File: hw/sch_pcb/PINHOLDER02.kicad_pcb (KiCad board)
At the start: 2 copper layers, 60.6 x 60.4 mm, 7 parts, among them J1 HEADER_1x03, M2 HOLE, M3 HOLE, M4 HOLE

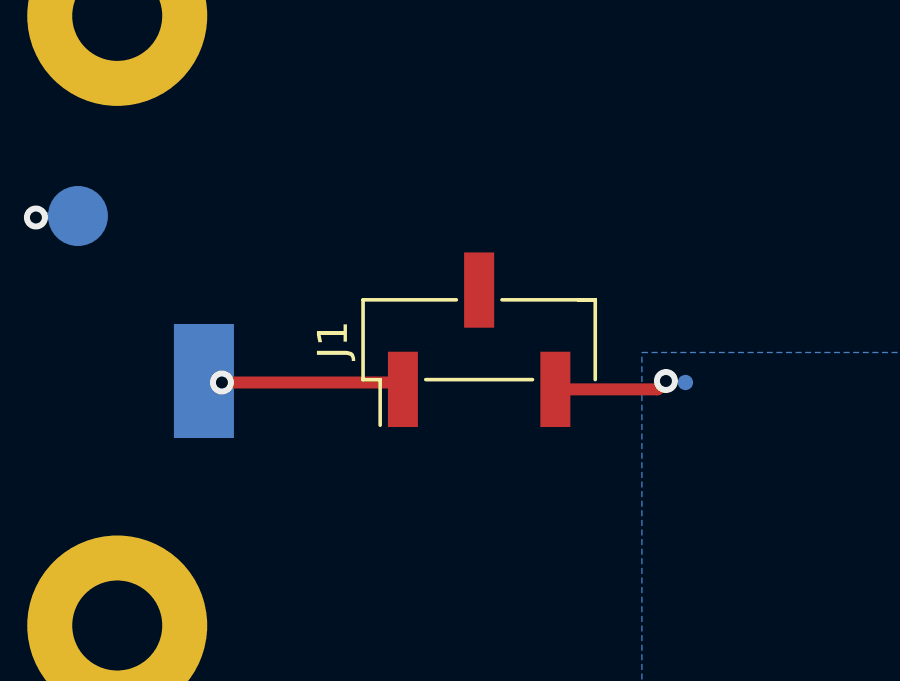
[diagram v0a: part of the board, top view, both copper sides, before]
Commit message: zamena anoda-katoda
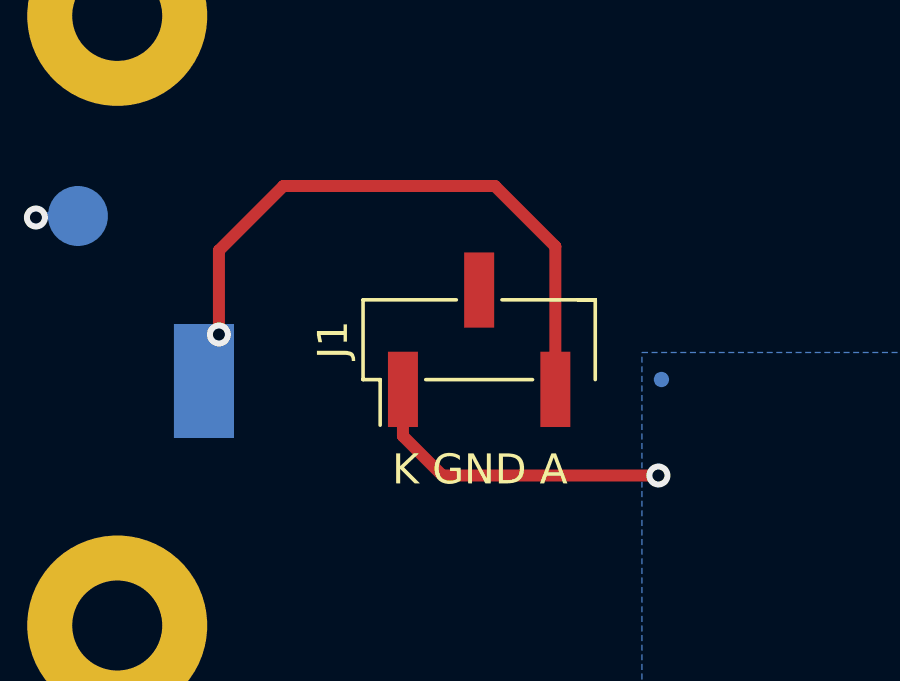
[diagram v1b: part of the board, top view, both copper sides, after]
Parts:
- moved TP1 0.81 mm to (167.8, 88.6)
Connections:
- J1 pad 1: Net-(J1-Pad1) -> /circle_0
- J1 pad 3: /circle_0 -> Net-(J1-Pad3)
- TP2 pad 1: Net-(J1-Pad1) -> Net-(J1-Pad3)
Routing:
- net Net-(J1-Pad3): track 0.00 -> 20.5 mm, vias 0 -> 1
- net /circle_0: track 3.87 -> 10.9 mm
- net Net-(J1-Pad1): track 6.13 -> 0.00 mm, vias 1 -> 0
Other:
- board text added: "A"
- board text added: "K GND A"
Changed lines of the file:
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@@
   (net 1 "/circle_0")
   (net 2 "GND")
-  (net 3 "Net-(J1-Pad1)")
+  (net 3 "Net-(J1-Pad3)")
   (footprint "Mlab_Mechanical:MountingHole_3mm" placed (layer "F.Cu")
     (at 149.61 76.48)
@@
     (fp_line (start 2.54 0.32) (end 1.27 0.32) (layer "F.Fab") (width 0.1))
     (pad "1" smd rect locked (at -1.655 -2.54 90) (size 2.51 1) (layers "F.Cu" "F.Paste" "F.Mask")
-      (net 3 "Net-(J1-Pad1)") (pintype "input"))
+      (net 1 "/circle_0") (pintype "input"))
     (pad "2" smd rect locked (at 1.655 0 90) (size 2.51 1) (layers "F.Cu" "F.Paste" "F.Mask")
       (net 2 "GND") (pintype "input"))
     (pad "3" smd rect locked (at -1.655 2.54 90) (size 2.51 1) (layers "F.Cu" "F.Paste" "F.Mask")
-      (net 1 "/circle_0") (pintype "input"))
+      (net 3 "Net-(J1-Pad3)") (pintype "input"))
     (model "${KICAD6_3DMODEL_DIR}/Connector_PinHeader_2.54mm.3dshapes/PinHeader_1x03_P2.54mm_Vertical_SMD_Pin1Left.wrl"
       (offset (xyz 0 0 0))
@@
   )
   (footprint "Mlab_CON:TestPoint_Pad_D0.5mm_noSilk" (layer "B.Cu")
-    (at 168.55 88.7 180)
+    (at 167.75 88.6 180)
     (descr "SMD pad as test Point, diameter 1.0mm")
     (tags "test point SMD pad")
@@
     (fp_line (start 0 -0.5) (end 0 -1) (layer "B.Fab") (width 0.15))
     (pad "1" smd rect (at 0 0 90) (size 3.8 2) (layers "B.Cu" "B.Paste" "B.Mask")
-      (net 3 "Net-(J1-Pad1)") (pinfunction "1") (pintype "passive"))
+      (net 3 "Net-(J1-Pad3)") (pinfunction "1") (pintype "passive"))
     (model "${KICAD6_3DMODEL_DIR}/TestPoint.3dshapes/TestPoint_Keystone_5019_Minature.wrl"
       (offset (xyz 0 0 0))
@@
   )
   (gr_text "GND" (at 148.25 85.85) (layer "B.SilkS")
-    (effects (font (size 1.5 1.5) (thickness 0.3)) (justify mirror))
+    (effects (font (size 1 1) (thickness 0.25)) (justify mirror))
   )
   (gr_text "MLAB.cz" (at 160.024 74.8925) (layer "B.SilkS")
     (effects (font (size 1.5 1.5) (thickness 0.3)) (justify mirror))
   )
+  (gr_text "A" (at 150.25 88.85 90) (layer "B.SilkS")
+    (effects (font (size 1 1) (thickness 0.15)) (justify mirror))
+  )
   (gr_text "PINHOLDER02A" (at 175.5 74.8) (layer "F.SilkS")
     (effects (font (size 1.7 1.7) (thickness 0.3)))
@@
     (effects (font (size 1.5 1.5) (thickness 0.3)))
   )
-  (segment (start 164.214 88.929) (end 167.621 88.929) (width 0.4) (layer "F.Cu") (net 1))
-  (segment (start 167.621 88.929) (end 167.9 88.65) (width 0.4) (layer "F.Cu") (net 1))
-  (via (at 167.9 88.65) (size 0.8) (drill 0.4) (layers "F.Cu" "B.Cu") (net 1))
-  (segment (start 167.95 88.7) (end 167.9 88.65) (width 0.25) (layer "B.Cu") (net 1))
+  (gr_text "K GND A" (at 161.7 91.6) (layer "F.SilkS")
+    (effects (font (size 1 1) (thickness 0.15)))
+  )
+  (segment (start 167.65 91.8) (end 160.45 91.8) (width 0.4) (layer "F.Cu") (net 1))
+  (segment (start 160.45 91.8) (end 159.134 90.484) (width 0.4) (layer "F.Cu") (net 1))
+  (segment (start 159.134 88.929) (end 158.905 88.7) (width 0.4) (layer "F.Cu") (net 1))
+  (segment (start 159.134 90.484) (end 159.134 88.929) (width 0.4) (layer "F.Cu") (net 1))
+  (via (at 167.65 91.8) (size 0.8) (drill 0.4) (layers "F.Cu" "B.Cu") (net 1))
   (via (at 146.9 83.2) (size 0.8) (drill 0.4) (layers "F.Cu" "B.Cu") (net 2))
   (segment (start 146.9 83.2) (end 146.95 83.15) (width 0.25) (layer "B.Cu") (net 2))
   (segment (start 146.95 83.15) (end 148.3 83.15) (width 0.25) (layer "B.Cu") (net 2))
-  (segment (start 158.905 88.7) (end 153.1 88.7) (width 0.4) (layer "F.Cu") (net 3))
-  (segment (start 159.134 88.929) (end 158.905 88.7) (width 0.4) (layer "F.Cu") (net 3))
-  (via (at 153.1 88.7) (size 0.8) (drill 0.4) (layers "F.Cu" "B.Cu") (net 3))
+  (segment (start 153 87.1) (end 153 84.3) (width 0.4) (layer "F.Cu") (net 3))
+  (segment (start 155.15 82.15) (end 162.2 82.15) (width 0.4) (layer "F.Cu") (net 3))
+  (segment (start 164.214 84.164) (end 164.214 88.929) (width 0.4) (layer "F.Cu") (net 3))
+  (segment (start 162.2 82.15) (end 164.214 84.164) (width 0.4) (layer "F.Cu") (net 3))
+  (segment (start 153 84.3) (end 155.15 82.15) (width 0.4) (layer "F.Cu") (net 3))
+  (via (at 153 87.1) (size 0.8) (drill 0.4) (layers "F.Cu" "B.Cu") (net 3))
   (zone (net 2) (net_name "GND") (layer "F.Cu") (hatch edge 0.508)
     (connect_pads (clearance 0.4))

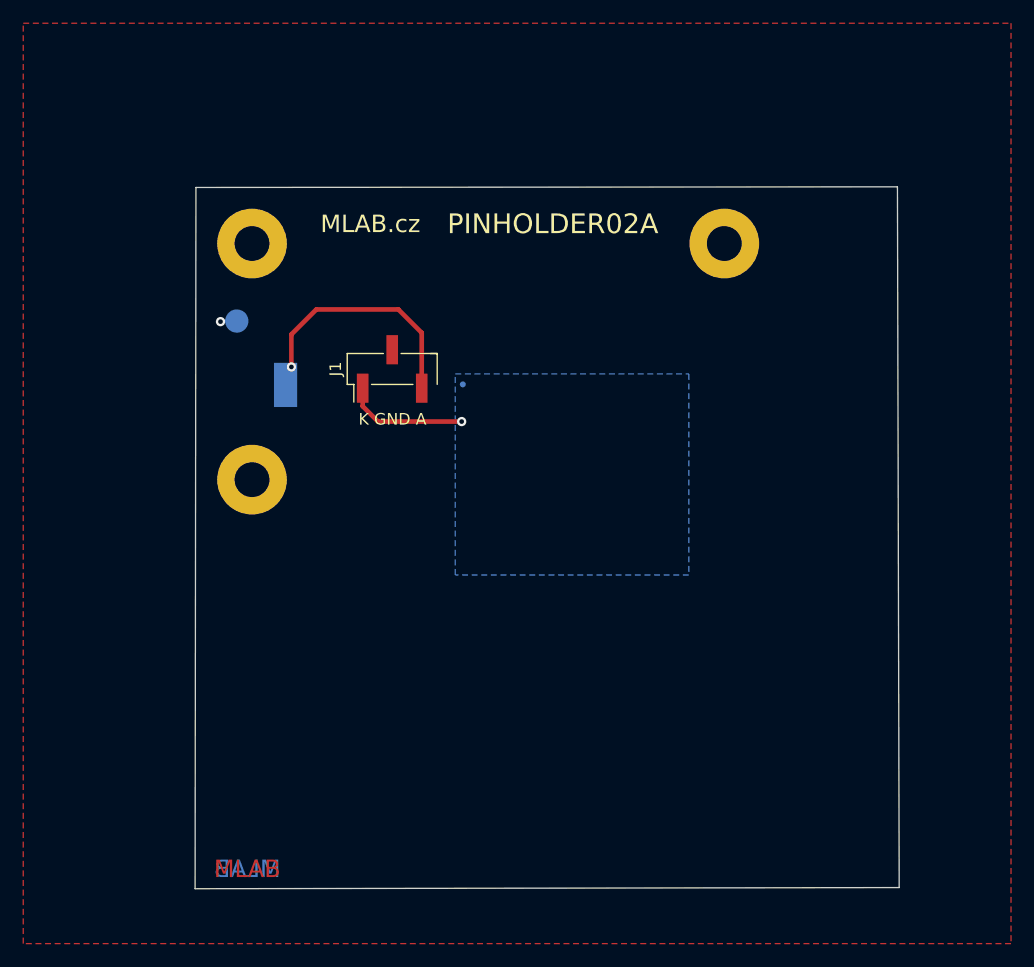
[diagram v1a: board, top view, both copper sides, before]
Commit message: Fix shape to be ortogonal.
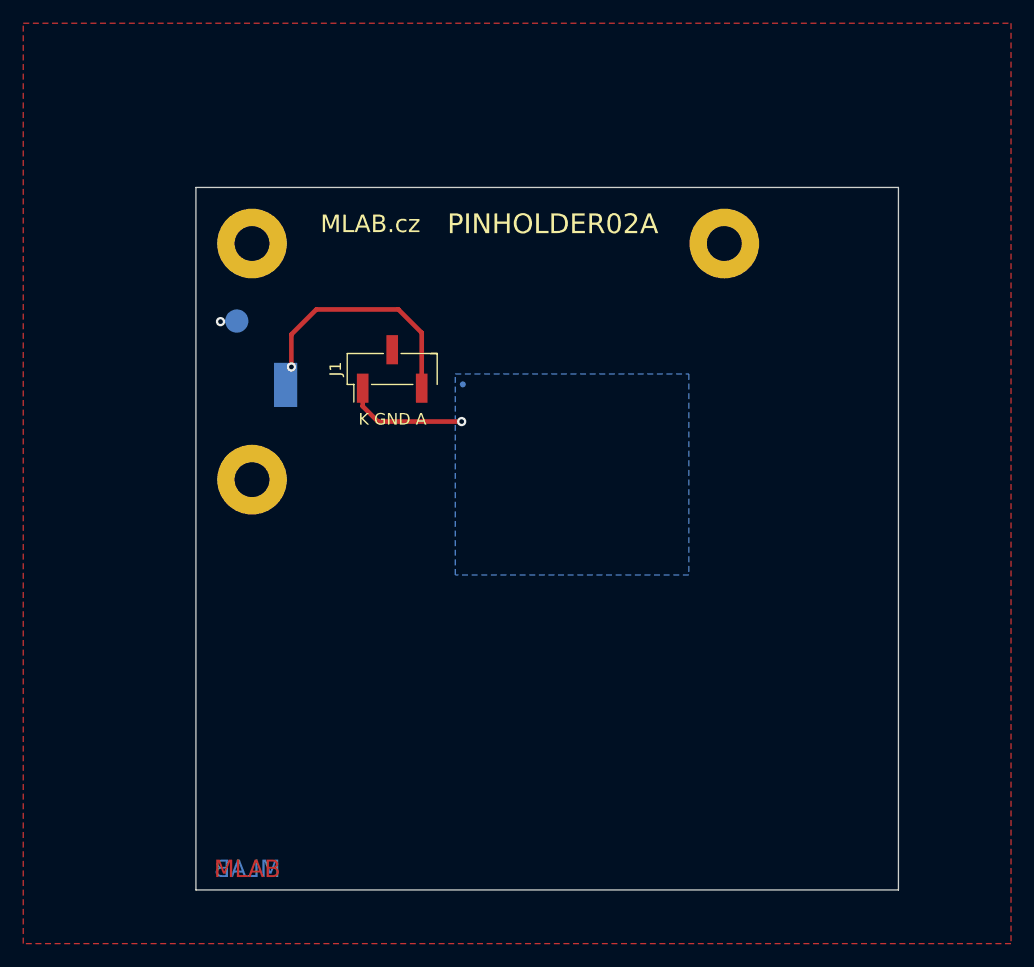
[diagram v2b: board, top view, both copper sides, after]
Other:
- board size 60.6 x 60.4 mm -> 60.5 x 60.5 mm
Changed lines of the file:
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@@
   (setup
     (pad_to_mask_clearance 0)
+    (aux_axis_origin 149.61 76.48)
     (pcbplotparams
       (layerselection 0x00010fc_ffffffff)
@@
     )
   )
-  (gr_line (start 144.712 132) (end 205.3 131.9) (layer "Edge.Cuts") (width 0.1))
-  (gr_line (start 144.786 71.656) (end 205.15 71.6) (layer "Edge.Cuts") (width 0.1))
-  (gr_line (start 205.15 71.6) (end 205.3 131.9) (layer "Edge.Cuts") (width 0.1))
-  (gr_line (start 144.712 132) (end 144.786 71.656) (layer "Edge.Cuts") (width 0.1))
+  (gr_line (start 144.784 132.106) (end 205.236 132.106) (layer "Edge.Cuts") (width 0.1))
+  (gr_line (start 144.784 71.654) (end 205.236 71.654) (layer "Edge.Cuts") (width 0.1))
+  (gr_line (start 205.236 71.654) (end 205.236 132.106) (layer "Edge.Cuts") (width 0.1))
+  (gr_line (start 144.784 132.106) (end 144.784 71.654) (layer "Edge.Cuts") (width 0.1))
   (gr_rect (start 134.8 78.6) (end 146.2 90.4) (layer "User.1") (width 0.15) (fill solid))
   (gr_line (start 146.6 78.2) (end 146.6 90.8) (layer "User.2") (width 1))
@@
     (effects (font (size 1 1) (thickness 0.15)))
   )
+  (dimension (type aligned) (layer "Cmts.User")
+    (pts (xy 144.784 132.106) (xy 205.236 132.106))
+    (height 3.784)
+    (gr_text "60,4520 mm" (at 175.01 134.74) (layer "Cmts.User")
+      (effects (font (size 1 1) (thickness 0.15)))
+    )
+    (format (units 3) (units_format 1) (precision 4))
+    (style (thickness 0.15) (arrow_length 1.27) (text_position_mode 0) (extension_height 0.58642) (extension_offset 0.5) keep_text_aligned)
+  )
+  (dimension (type aligned) (layer "Cmts.User")
+    (pts (xy 144.784 71.654) (xy 205.236 71.654))
+    (height -6.884)
+    (gr_text "60,4520 mm" (at 175.01 63.62) (layer "Cmts.User")
+      (effects (font (size 1 1) (thickness 0.15)))
+    )
+    (format (units 3) (units_format 1) (precision 4))
+    (style (thickness 0.15) (arrow_length 1.27) (text_position_mode 0) (extension_height 0.58642) (extension_offset 0.5) keep_text_aligned)
+  )
+  (dimension (type aligned) (layer "Cmts.User")
+    (pts (xy 205.236 132.106) (xy 205.236 71.654))
+    (height 6.854)
+    (gr_text "60,4520 mm" (at 210.94 101.88 90) (layer "Cmts.User")
+      (effects (font (size 1 1) (thickness 0.15)))
+    )
+    (format (units 3) (units_format 1) (precision 4))
+    (style (thickness 0.15) (arrow_length 1.27) (text_position_mode 0) (extension_height 0.58642) (extension_offset 0.5) keep_text_aligned)
+  )
+  (dimension (type aligned) (layer "Cmts.User")
+    (pts (xy 149.61 76.48) (xy 149.61 96.8))
+    (height 11.18)
+    (gr_text "20,3200 mm" (at 137.28 86.64 90) (layer "Cmts.User")
+      (effects (font (size 1 1) (thickness 0.15)))
+    )
+    (format (units 3) (units_format 1) (precision 4))
+    (style (thickness 0.15) (arrow_length 1.27) (text_position_mode 0) (extension_height 0.58642) (extension_offset 0.5) keep_text_aligned)
+  )
+  (dimension (type aligned) (layer "Cmts.User")
+    (pts (xy 144.784 132.106) (xy 144.784 71.654))
+    (height -10.164)
+    (gr_text "60,4520 mm" (at 133.47 101.88 90) (layer "Cmts.User")
+      (effects (font (size 1 1) (thickness 0.15)))
+    )
+    (format (units 3) (units_format 1) (precision 4))
+    (style (thickness 0.15) (arrow_length 1.27) (text_position_mode 0) (extension_height 0.58642) (extension_offset 0.5) keep_text_aligned)
+  )
+  (dimension (type aligned) (layer "Cmts.User")
+    (pts (xy 149.61 76.48) (xy 190.25 76.48))
+    (height -9.17)
+    (gr_text "40,6400 mm" (at 169.93 66.16) (layer "Cmts.User")
+      (effects (font (size 1 1) (thickness 0.15)))
+    )
+    (format (units 3) (units_format 1) (precision 4))
+    (style (thickness 0.15) (arrow_length 1.27) (text_position_mode 0) (extension_height 0.58642) (extension_offset 0.5) keep_text_aligned)
+  )
   (segment (start 167.65 91.8) (end 160.45 91.8) (width 0.4) (layer "F.Cu") (net 1))

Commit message: Edit PCB
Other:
- rule pad_to_mask_clearance: 0 -> 0.2
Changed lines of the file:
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@@
   )
   (setup
-    (pad_to_mask_clearance 0)
+    (stackup
+      (layer "F.SilkS" (type "Top Silk Screen"))
+      (layer "F.Paste" (type "Top Solder Paste"))
+      (layer "F.Mask" (type "Top Solder Mask") (thickness 0.01))
+      (layer "F.Cu" (type "copper") (thickness 0.035))
+      (layer "dielectric 1" (type "core") (thickness 1.51) (material "FR4") (epsilon_r 4.5) (loss_tangent 0.02))
+      (layer "B.Cu" (type "copper") (thickness 0.035))
+      (layer "B.Mask" (type "Bottom Solder Mask") (thickness 0.01))
+      (layer "B.Paste" (type "Bottom Solder Paste"))
+      (layer "B.SilkS" (type "Bottom Silk Screen"))
+      (copper_finish "None")
+      (dielectric_constraints no)
+    )
+    (pad_to_mask_clearance 0.2)
     (aux_axis_origin 149.61 76.48)
     (pcbplotparams
